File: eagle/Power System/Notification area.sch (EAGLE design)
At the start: 53 parts, among them IC3 LM358N, T7 2N2222

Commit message: PCB layout beta
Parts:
- removed D5, D6, D7, D8: 1N4004, diode:1N4004
- removed S1, S2: RDT1034, switch:RDT1034
- removed S4: TL32PO, switch:TL32PO
- added C8, C9: 2uF, capacitor-wima:C2,5-3
- added LED_A: BLUE, display-hp:HLMP6
- added LED_B, LED_D: GREEN, display-hp:HLMP6
- added LED_C: RED, display-hp:HLMP6
- added PAD3: Power +, wirepad:WIREPADSMD5-2,5
- added PAD4: Power -, wirepad:WIREPADSMD5-2,5
- added SV2: (no value), con-lstb:MA03-1
- C4, C7: value 1uF -> 2uF
- D1, D2: value HLMP6 -> 1N4001; device display-hp:HLMP6 -> diode:1N4004
- D3, D4: value HLMP6 -> 1N4004; device display-hp:HLMP6 -> diode:1N4004
- PAD1: value WIREPADSMD5-2,5 -> Motor +
- PAD2: value WIREPADSMD5-2,5 -> Motor -
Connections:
- removed net N$15: S1.B, S2.B
- new net N$29: R20.1, T7.B
- new net N$30: C8.2, C9.1
- new net N$31: R7.2, T4.C
- new net N$32: R1.1, T1.C
- new net N$33: R3.2, T2.C
- net +3V3: now also D2.C, LED_A.A, LED_B.A, LED_C.A, LED_D.A; no longer D2.A, D3.A, D4.A, D5.C, D6.A
- net +5V: now also C8.1, D3.A, D4.C; no longer C7.1, D7.C, D8.A
- net GND: now also C9.2, IC3P.V-, PAD4.P, SV2.3; no longer C4.2
- net N$1: now also LED_C.K; no longer D1.K
- net N$13: now also SV2.1; no longer S1.A, S2.A
- net N$14: now also R5.1, T3.C; no longer C2.1, C5.1, D6.C, D8.C, IC1.IN, IC2.IN, PAD1.P, S4.P
- net N$17: now also C4.2, C7.1; no longer S1.A1, S2.A1
- net N$19: now also D2.A; no longer D5.A
- net N$20: now also D4.A; no longer D7.A
- net N$28: now also R20.2; no longer R20.1, T7.B
- net N$3: now also LED_D.K; no longer D2.K
- net N$5: now also LED_A.K; no longer D3.K
- net N$7: now also LED_B.K; no longer D4.K
- net V+: now also C2.1, C5.1, D1.C, D3.C, IC1.IN, IC2.IN, IC3P.V+, PAD1.P, PAD3.P; no longer S4.S
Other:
- moved on the sheet: C7, R20

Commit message: updated pcb
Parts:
- SG1: value F/BC35 -> F/DB18; device buzzer:F/BC35 -> buzzer:F/DB18
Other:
- note added: "Autonomous Mode - Red"
- note removed: "Battery Empty - Red"
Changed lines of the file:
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@@
 <?xml version="1.0" encoding="utf-8"?>
 <!DOCTYPE eagle SYSTEM "eagle.dtd">
-<eagle version="7.5.0">
+<eagle version="7.3.0">
 <drawing>
 <settings>
@@
 <part name="P+2" library="supply1" deviceset="+5V" device=""/>
 <part name="T5" library="transistor-neu-to92" deviceset="*-NPN-" device="TO92-EBC" technology="2N2222"/>
-<part name="SG1" library="buzzer" deviceset="F/BC35" device=""/>
 <part name="GND10" library="supply1" deviceset="GND" device=""/>
 <part name="P+1" library="supply1" deviceset="V+" device="" value="9.6V"/>
@@
 <part name="P+6" library="supply1" deviceset="V+" device="" value="9.6V"/>
 <part name="GND13" library="supply1" deviceset="GND" device=""/>
+<part name="SG1" library="buzzer" deviceset="F/DB18" device=""/>
 </parts>
 <sheets>
@@
 <text x="55.88" y="177.8" size="1.778" layer="92">Bluetooth - Blue</text>
 <text x="78.74" y="177.8" size="1.778" layer="92">Battery Ok - Green</text>
-<text x="104.14" y="177.8" size="1.778" layer="92">Battery Empty - Red</text>
+<text x="101.6" y="177.8" size="1.778" layer="92">Autonomous Mode - Red</text>
 <text x="129.54" y="177.8" size="1.778" layer="92">System Ok - Green</text>
 </plain>
@@
 <instance part="GND9" gate="1" x="-33.02" y="165.1"/>
 <instance part="P+2" gate="1" x="15.24" y="203.2"/>
-<instance part="T5" gate="G$1" x="180.34" y="198.12"/>
-<instance part="SG1" gate="G$1" x="180.34" y="208.28" rot="R90"/>
+<instance part="T5" gate="G$1" x="180.34" y="198.12" smashed="yes">
+<attribute name="NAME" x="182.88" y="198.12" size="1.778" layer="95"/>
+<attribute name="VALUE" x="170.18" y="203.2" size="1.778" layer="96"/>
+</instance>
 <instance part="GND10" gate="1" x="175.26" y="190.5"/>
 <instance part="P+1" gate="1" x="-116.84" y="302.26"/>
@@
 <instance part="P+6" gate="1" x="-101.6" y="200.66"/>
 <instance part="GND13" gate="1" x="144.78" y="251.46"/>
+<instance part="SG1" gate="G$1" x="180.34" y="208.28" smashed="yes" rot="R90">
+<attribute name="NAME" x="173.99" y="208.28" size="1.778" layer="95" rot="R90"/>
+<attribute name="VALUE" x="175.26" y="215.9" size="1.778" layer="96" rot="R90"/>
+</instance>
 </instances>
 <busses>
@@
 </segment>
 <segment>
-<pinref part="SG1" gate="G$1" pin="-"/>
 <pinref part="P+3" gate="1" pin="+5V"/>
 <wire x1="182.88" y1="218.44" x2="182.88" y2="215.9" width="0.1524" layer="91"/>
@@
 <wire x1="187.96" y1="215.9" x2="187.96" y2="210.82" width="0.1524" layer="91"/>
 <junction x="182.88" y="215.9"/>
+<pinref part="SG1" gate="G$1" pin="-"/>
 </segment>
 </net>
@@
 <segment>
 <pinref part="T5" gate="G$1" pin="C"/>
-<pinref part="SG1" gate="G$1" pin="+"/>
 <wire x1="182.88" y1="205.74" x2="182.88" y2="203.2" width="0.1524" layer="91"/>
 <pinref part="D9" gate="1" pin="A"/>
@@
 <wire x1="187.96" y1="203.2" x2="182.88" y2="203.2" width="0.1524" layer="91"/>
 <junction x="182.88" y="203.2"/>
-</segment>
-</net>
+<pinref part="SG1" gate="G$1" pin="+"/>
+</segment>
+</net>

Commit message: final pcb versions
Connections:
- new net N$34: R10.1, SV2.2
- net N$12: now also SV1.6; no longer SV1.7
- net N$13: no longer R10.1
- net N$18: now also SV1.7; no longer SV1.6
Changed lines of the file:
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@@
 <?xml version="1.0" encoding="utf-8"?>
 <!DOCTYPE eagle SYSTEM "eagle.dtd">
-<eagle version="7.3.0">
+<eagle version="7.5.0">
 <drawing>
 <settings>
@@
 <wire x1="116.84" y1="223.52" x2="68.58" y2="223.52" width="0.1524" layer="91"/>
 <wire x1="68.58" y1="223.52" x2="68.58" y2="238.76" width="0.1524" layer="91"/>
-<pinref part="SV1" gate="G$1" pin="7"/>
-<wire x1="68.58" y1="238.76" x2="60.96" y2="238.76" width="0.1524" layer="91"/>
-<wire x1="60.96" y1="238.76" x2="60.96" y2="271.78" width="0.1524" layer="91"/>
+<wire x1="68.58" y1="238.76" x2="58.42" y2="238.76" width="0.1524" layer="91"/>
+<pinref part="SV1" gate="G$1" pin="6"/>
+<wire x1="58.42" y1="238.76" x2="58.42" y2="271.78" width="0.1524" layer="91"/>
 </segment>
 </net>
@@
 <net name="N$13" class="0">
 <segment>
-<pinref part="R10" gate="G$1" pin="1"/>
 <pinref part="R9" gate="G$1" pin="1"/>
-<wire x1="127" y1="251.46" x2="132.08" y2="251.46" width="0.1524" layer="91"/>
-<wire x1="132.08" y1="251.46" x2="132.08" y2="256.54" width="0.1524" layer="91"/>
-<wire x1="132.08" y1="251.46" x2="139.7" y2="251.46" width="0.1524" layer="91"/>
-<junction x="132.08" y="251.46"/>
+<wire x1="132.08" y1="254" x2="132.08" y2="256.54" width="0.1524" layer="91"/>
+<wire x1="132.08" y1="254" x2="139.7" y2="254" width="0.1524" layer="91"/>
 <pinref part="SV2" gate="G$1" pin="1"/>
-<wire x1="139.7" y1="251.46" x2="139.7" y2="254" width="0.1524" layer="91"/>
 </segment>
 </net>
@@
 <wire x1="99.06" y1="220.98" x2="66.04" y2="220.98" width="0.1524" layer="91"/>
 <wire x1="66.04" y1="220.98" x2="66.04" y2="236.22" width="0.1524" layer="91"/>
-<pinref part="SV1" gate="G$1" pin="6"/>
-<wire x1="66.04" y1="236.22" x2="58.42" y2="236.22" width="0.1524" layer="91"/>
-<wire x1="58.42" y1="236.22" x2="58.42" y2="271.78" width="0.1524" layer="91"/>
+<wire x1="66.04" y1="236.22" x2="60.96" y2="236.22" width="0.1524" layer="91"/>
+<pinref part="SV1" gate="G$1" pin="7"/>
+<wire x1="60.96" y1="236.22" x2="60.96" y2="271.78" width="0.1524" layer="91"/>
 </segment>
 </net>
@@
 </segment>
 </net>
+<net name="N$34" class="0">
+<segment>
+<pinref part="R10" gate="G$1" pin="1"/>
+<pinref part="SV2" gate="G$1" pin="2"/>
+<wire x1="127" y1="251.46" x2="142.24" y2="251.46" width="0.1524" layer="91"/>
+<wire x1="142.24" y1="251.46" x2="142.24" y2="254" width="0.1524" layer="91"/>
+</segment>
+</net>

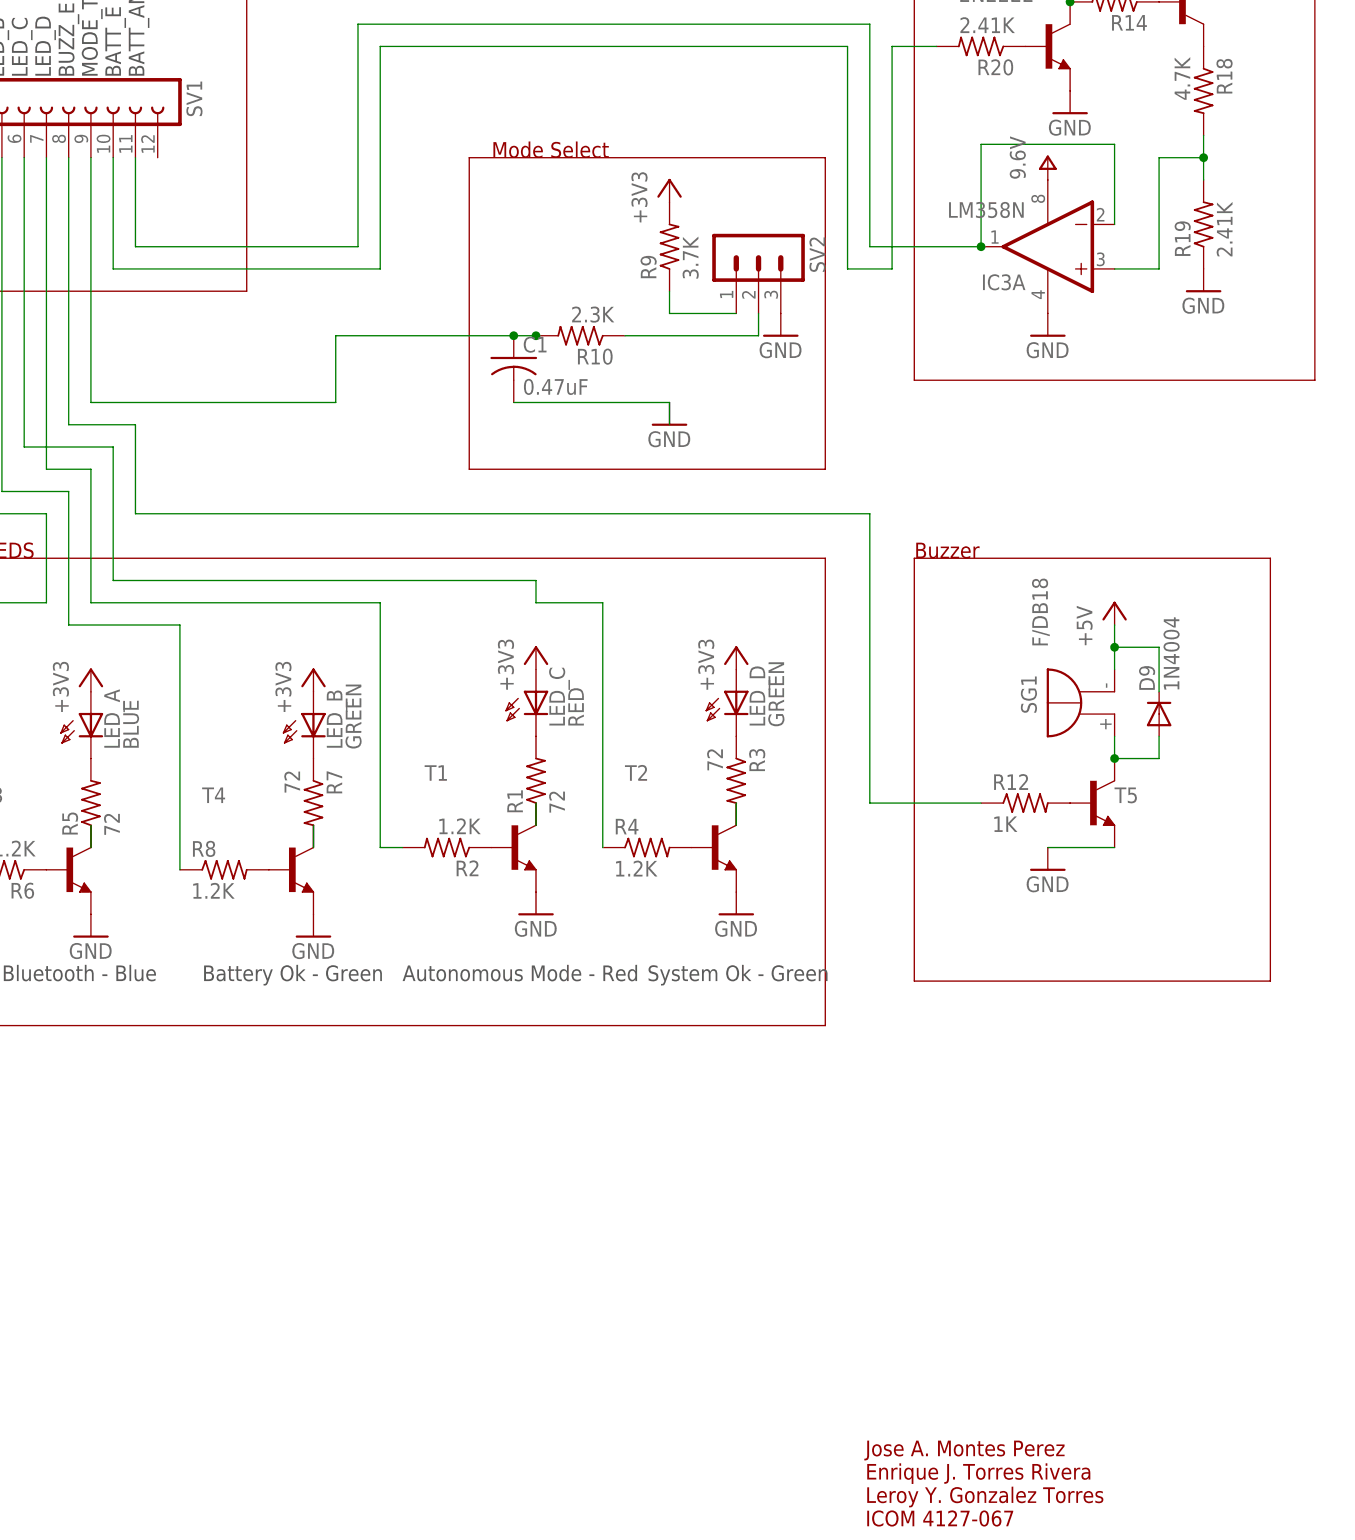
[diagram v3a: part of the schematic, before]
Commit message: added multimeter
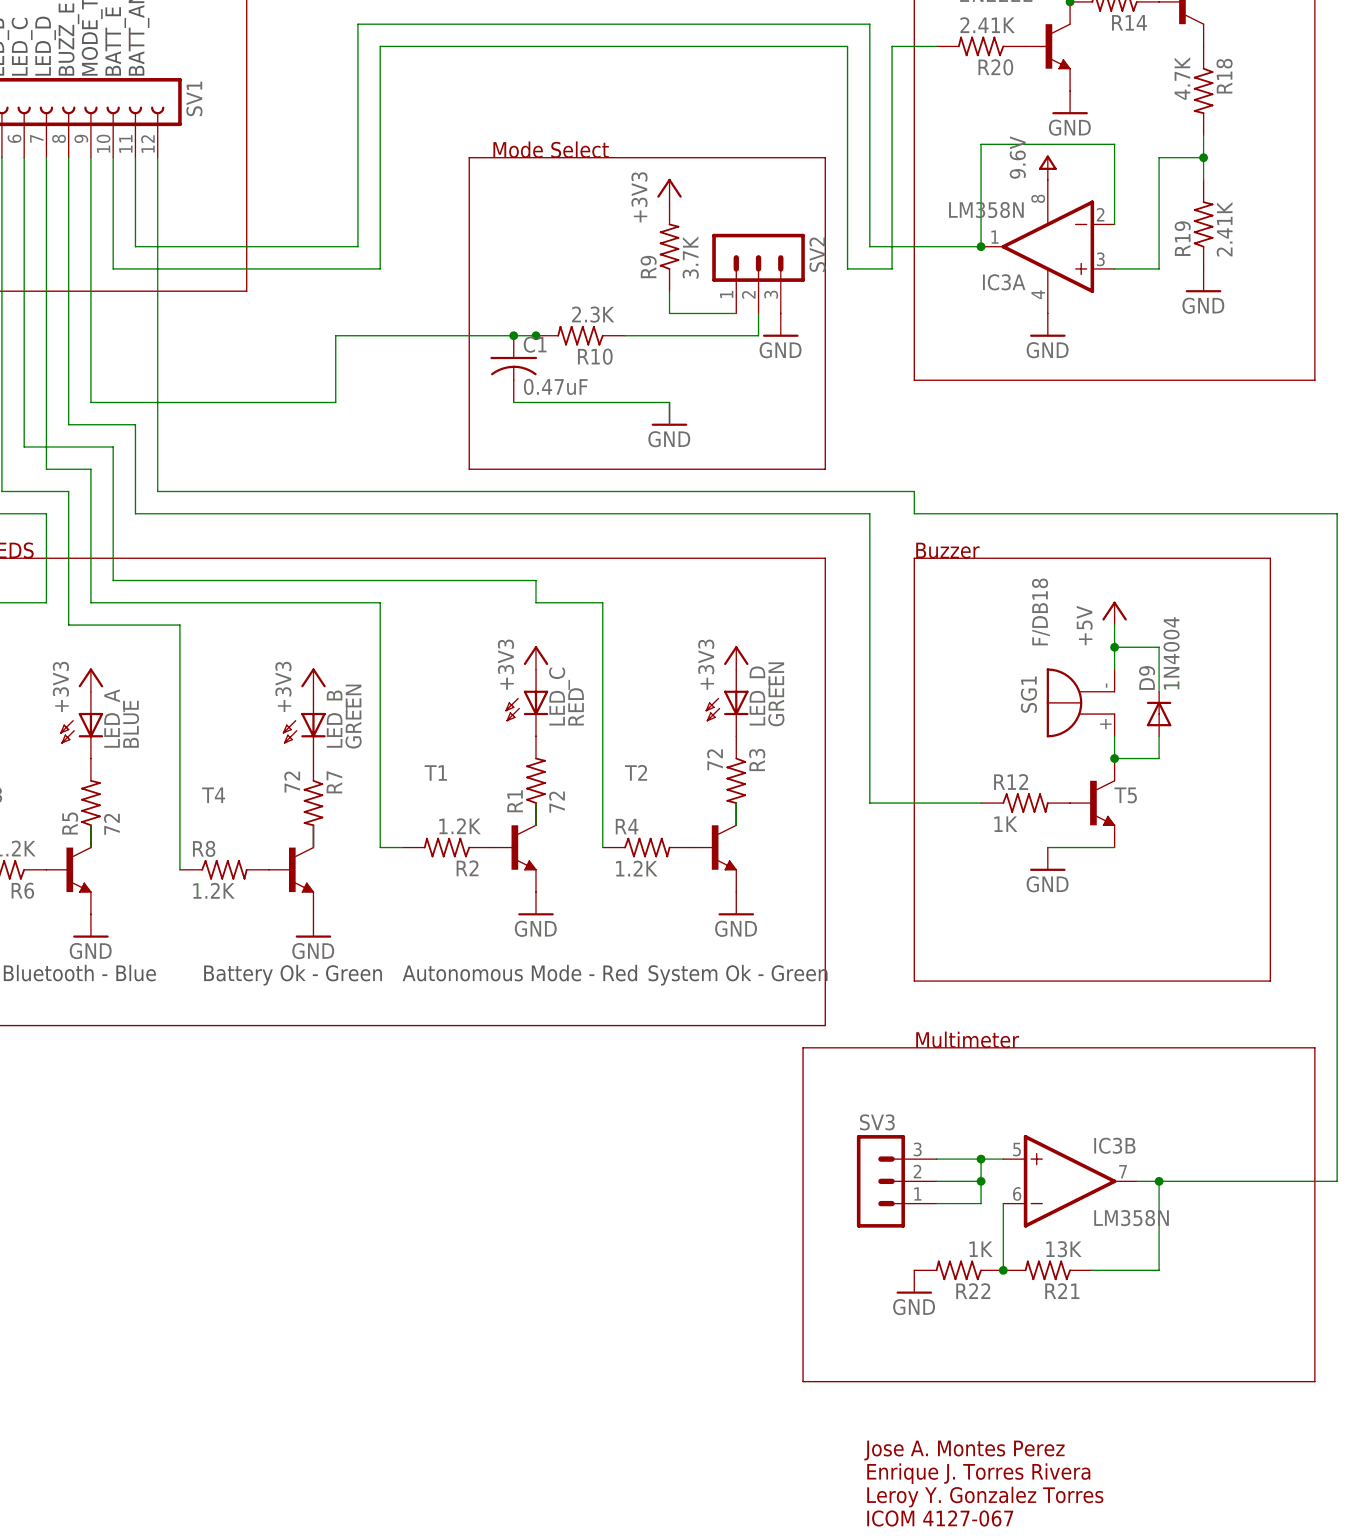
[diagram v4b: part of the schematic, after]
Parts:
- added R21: 13K, rcl:R-US_0204/7
- added R22: 1K, rcl:R-US_0204/7
- added SV3: (no value), con-lstb:MA03-1
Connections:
- new net N$35: IC3B.-IN, R21.2, R22.1
- new net N$36: IC3B.OUT, R21.1, SV1.12
- new net N$37: IC3B.+IN, SV3.1, SV3.2, SV3.3
- net GND: now also R22.2
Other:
- note added: "Multimeter"
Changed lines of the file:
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@@
 <?xml version="1.0" encoding="utf-8"?>
 <!DOCTYPE eagle SYSTEM "eagle.dtd">
-<eagle version="7.5.0">
+<eagle version="7.3.0">
 <drawing>
 <settings>
@@
 <part name="GND13" library="supply1" deviceset="GND" device=""/>
 <part name="SG1" library="buzzer" deviceset="F/DB18" device=""/>
+<part name="R21" library="rcl" deviceset="R-US_" device="0204/7" value="13K"/>
+<part name="R22" library="rcl" deviceset="R-US_" device="0204/7" value="1K"/>
+<part name="GND14" library="supply1" deviceset="GND" device=""/>
+<part name="SV3" library="con-lstb" deviceset="MA03-1" device=""/>
 </parts>
 <sheets>
@@
 <text x="101.6" y="177.8" size="1.778" layer="92">Autonomous Mode - Red</text>
 <text x="129.54" y="177.8" size="1.778" layer="92">System Ok - Green</text>
+<wire x1="147.32" y1="170.18" x2="147.32" y2="132.08" width="0.1524" layer="94"/>
+<wire x1="147.32" y1="132.08" x2="205.74" y2="132.08" width="0.1524" layer="94"/>
+<wire x1="205.74" y1="132.08" x2="205.74" y2="170.18" width="0.1524" layer="94"/>
+<wire x1="205.74" y1="170.18" x2="147.32" y2="170.18" width="0.1524" layer="94"/>
+<text x="160.02" y="170.18" size="1.778" layer="94">Multimeter</text>
 </plain>
 <instances>
@@
 <attribute name="VALUE" x="175.26" y="215.9" size="1.778" layer="96" rot="R90"/>
 </instance>
+<instance part="IC3" gate="B" x="177.8" y="154.94"/>
+<instance part="R21" gate="G$1" x="175.26" y="144.78" rot="R180"/>
+<instance part="R22" gate="G$1" x="165.1" y="144.78" rot="R180"/>
+<instance part="GND14" gate="1" x="160.02" y="142.24"/>
+<instance part="SV3" gate="G$1" x="154.94" y="154.94"/>
 </instances>
 <busses>
@@
 <pinref part="GND13" gate="1" pin="GND"/>
 </segment>
+<segment>
+<pinref part="R22" gate="G$1" pin="2"/>
+<pinref part="GND14" gate="1" pin="GND"/>
+</segment>
 </net>
 <net name="N$2" class="0">
@@
 </segment>
 </net>
+<net name="N$36" class="0">
+<segment>
+<pinref part="IC3" gate="B" pin="OUT"/>
+<wire x1="185.42" y1="154.94" x2="187.96" y2="154.94" width="0.1524" layer="91"/>
+<wire x1="187.96" y1="154.94" x2="208.28" y2="154.94" width="0.1524" layer="91"/>
+<wire x1="208.28" y1="154.94" x2="208.28" y2="231.14" width="0.1524" layer="91"/>
+<wire x1="208.28" y1="231.14" x2="160.02" y2="231.14" width="0.1524" layer="91"/>
+<wire x1="160.02" y1="231.14" x2="160.02" y2="233.68" width="0.1524" layer="91"/>
+<pinref part="SV1" gate="G$1" pin="12"/>
+<wire x1="160.02" y1="233.68" x2="73.66" y2="233.68" width="0.1524" layer="91"/>
+<wire x1="73.66" y1="233.68" x2="73.66" y2="271.78" width="0.1524" layer="91"/>
+<pinref part="R21" gate="G$1" pin="1"/>
+<wire x1="180.34" y1="144.78" x2="187.96" y2="144.78" width="0.1524" layer="91"/>
+<wire x1="187.96" y1="144.78" x2="187.96" y2="154.94" width="0.1524" layer="91"/>
+<junction x="187.96" y="154.94"/>
+</segment>
+</net>
+<net name="N$37" class="0">
+<segment>
+<pinref part="SV3" gate="G$1" pin="3"/>
+<pinref part="IC3" gate="B" pin="+IN"/>
+<wire x1="162.56" y1="157.48" x2="167.64" y2="157.48" width="0.1524" layer="91"/>
+<pinref part="SV3" gate="G$1" pin="2"/>
+<wire x1="167.64" y1="157.48" x2="170.18" y2="157.48" width="0.1524" layer="91"/>
+<wire x1="162.56" y1="154.94" x2="167.64" y2="154.94" width="0.1524" layer="91"/>
+<wire x1="167.64" y1="154.94" x2="167.64" y2="157.48" width="0.1524" layer="91"/>
+<junction x="167.64" y="157.48"/>
+<pinref part="SV3" gate="G$1" pin="1"/>
+<wire x1="162.56" y1="152.4" x2="167.64" y2="152.4" width="0.1524" layer="91"/>
+<wire x1="167.64" y1="152.4" x2="167.64" y2="154.94" width="0.1524" layer="91"/>
+<junction x="167.64" y="154.94"/>
+</segment>
+</net>
+<net name="N$35" class="0">
+<segment>
+<pinref part="R21" gate="G$1" pin="2"/>
+<pinref part="R22" gate="G$1" pin="1"/>
+<pinref part="IC3" gate="B" pin="-IN"/>
+<wire x1="170.18" y1="152.4" x2="170.18" y2="144.78" width="0.1524" layer="91"/>
+<junction x="170.18" y="144.78"/>
+</segment>
+</net>

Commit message: last push
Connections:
- removed net N$28: R20.2, SV1.10
- new net N$39: IC3A.-IN, IC3A.OUT, SV1.10
- net N$26: now also R20.2; no longer IC3A.-IN, IC3A.OUT
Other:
- moved on the sheet: IC3A, LED_B, R14, R16, R18, R19, R20, R7, R8, T4, T6, T7
